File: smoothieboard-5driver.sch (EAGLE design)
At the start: 234 parts, among them IC1 LPC1769, IC10 LM1117-3.3V, IC11 78L12F, IC2 A4982, IC3 A4982, IC4 MCP44X1, IC5 A4982, IC6 A4982, J10 POWER_JACKSMD, Q1 BSL207SP, Q2 12MHz, Q3 25MHz, Q6 AOT240L, Q7 AOT240L, Q8 ZXMN4A06GTA, Q9 ZXMN4A06GTA, U1 USD-SOCKETNEW, X14 USBPTH

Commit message: Added 5th driver, 2nd digipot. Still lots of layout work to do
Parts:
- added C68, C69, C70, C71, C73: .1uF, rcl:C-EUC0603
- added C72: .22uF, rcl:C-EUC0603
- added C74: 100uF, SparkFun:CAP_POLE
- added IC12: A4982, A4982:A4982
- added IC9: MCP44X1, Geos:MCP44X1
- added J5: (no value), con-amp:MTA04-100
- added R18: 33K, resistor:R-US_R0603
- added R19, R20, R81: 10K, resistor:R-US_R0603
- added R21, R79: 0.05R, SparkFun:RESISTOR2512
- added R4: 100K, resistor:R-US_R0603
- added R80: NP, resistor:R-US_R0603
- added X5: (no value), con-weidmueller-sl35:180G-4
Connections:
- new net DIR5: IC12.DIR
- new net EN5: IC12.^EN
- new net N$29: IC9.!RESET, R4.1
- new net N$56: IC9.P0A, IC9.P1A, IC9.P2A, IC9.P3A, R18.1
- new net N$58: C69.2, IC12.CP1
- new net N$59: C69.1, IC12.CP2
- new net N$64: C70.2, IC12.VCP
- new net N$65: IC12.SENSE1, R21.2
- new net N$66: IC12.SENSE2, R79.2
- new net N$70: IC12.OUT1A, J5.2, X5.2
- new net N$71: IC12.OUT1B, J5.1, X5.1
- new net N$72: IC12.OUT2A, J5.3, X5.3
- new net N$76: IC12.OUT2B, J5.4, X5.4
- new net N$79: IC12.ROSC, R19.1, R80.1
- new net N$83: C72.2, IC12.VREG
- new net N$89: IC12.^SLEEP, R20.1
- new net N$95: IC12.^RESET, R81.1
- new net PW5: IC12.REF, IC9.P0W
- new net STEP5: IC12.STEP
- net 3.3V: now also C68.2, C71.1, IC12.VDD, IC9.HVC/A0, IC9.VDD, R18.2, R20.2, R4.2, R80.2, R81.2
- net GND: now also C68.1, C71.2, C72.1, C73.2, C74.-, IC12.GND1, IC12.GND2, IC12.PAD, IC9.A1, IC9.P0B, IC9.P1B, IC9.P2B, IC9.P3B, IC9.VSS, R19.2, R21.1, R79.1
- net MS1: now also IC12.MS1
- net MS2: now also IC12.MS2
- net POT_SCL: now also IC9.SCL
- net POT_SDA: now also IC9.SDA
- net VBB: now also C70.1, C73.1, C74.+, IC12.VBB1, IC12.VBB2

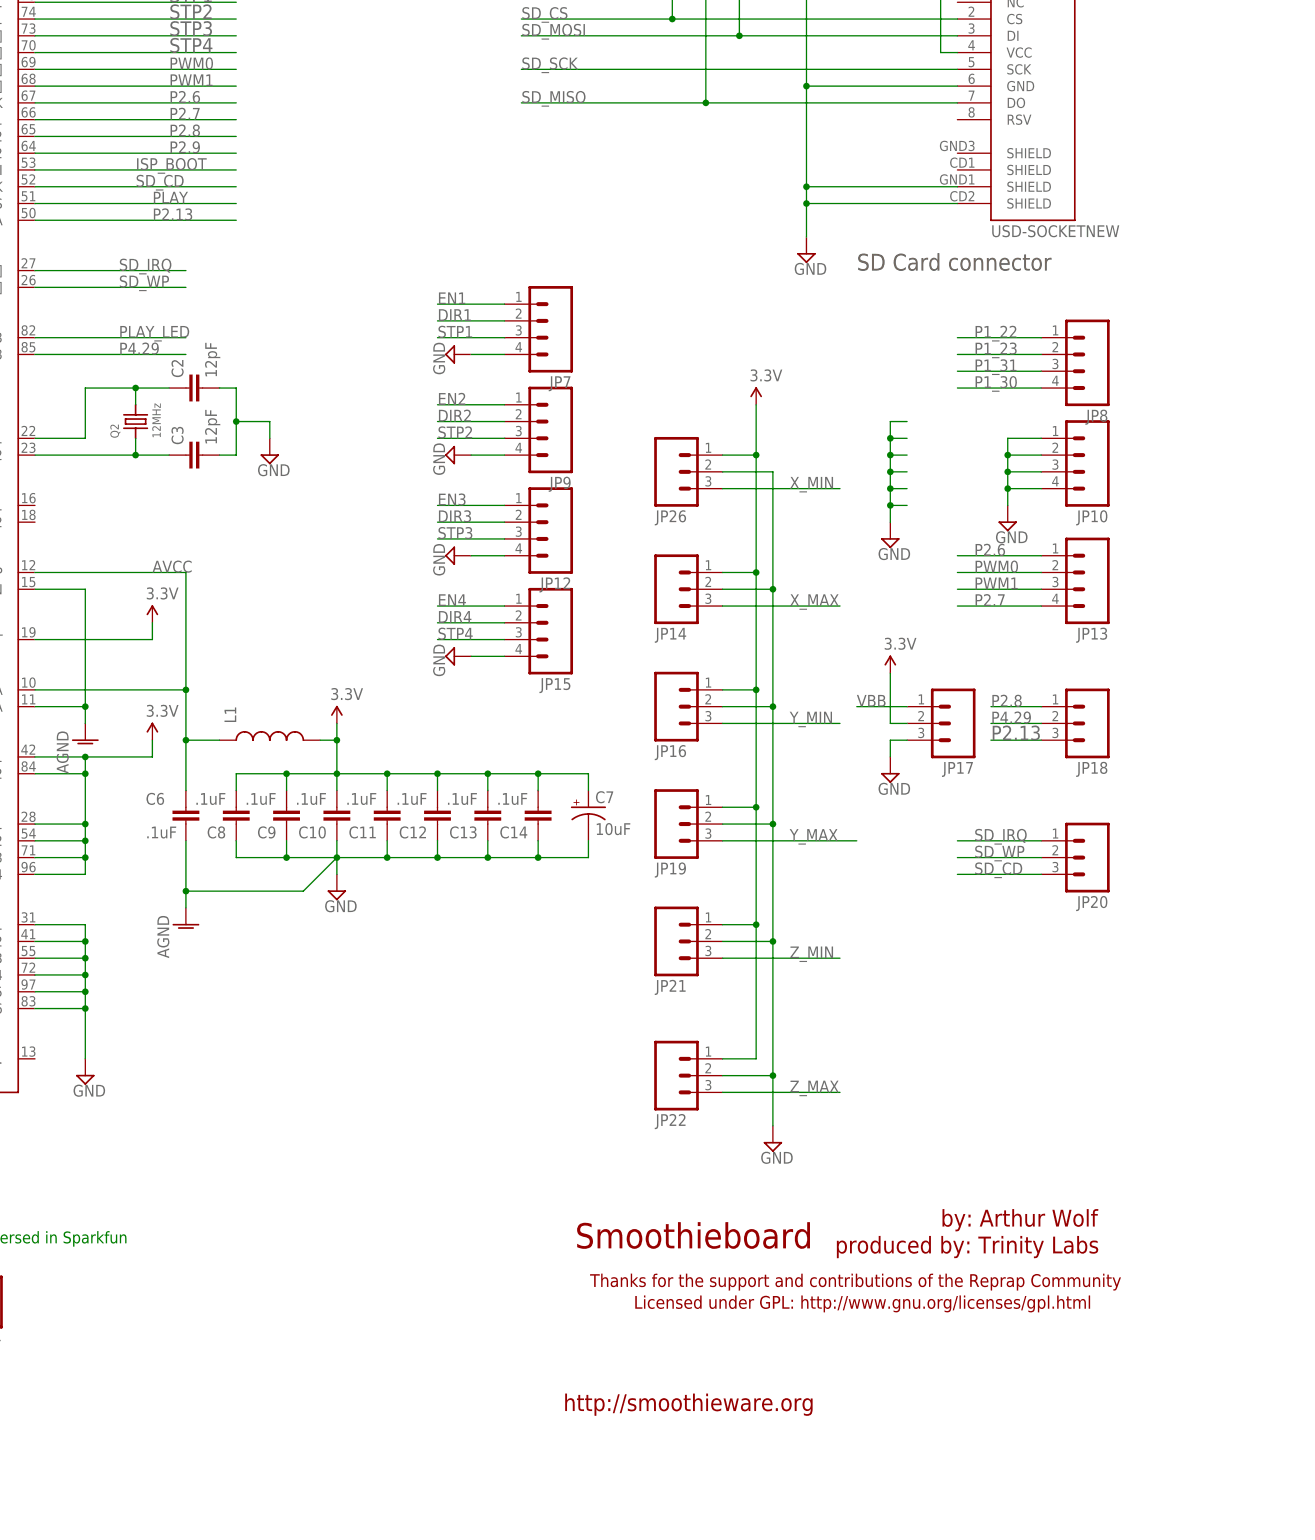
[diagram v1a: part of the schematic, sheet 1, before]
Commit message: shifted power connectors, lots of rearranging, still more to do
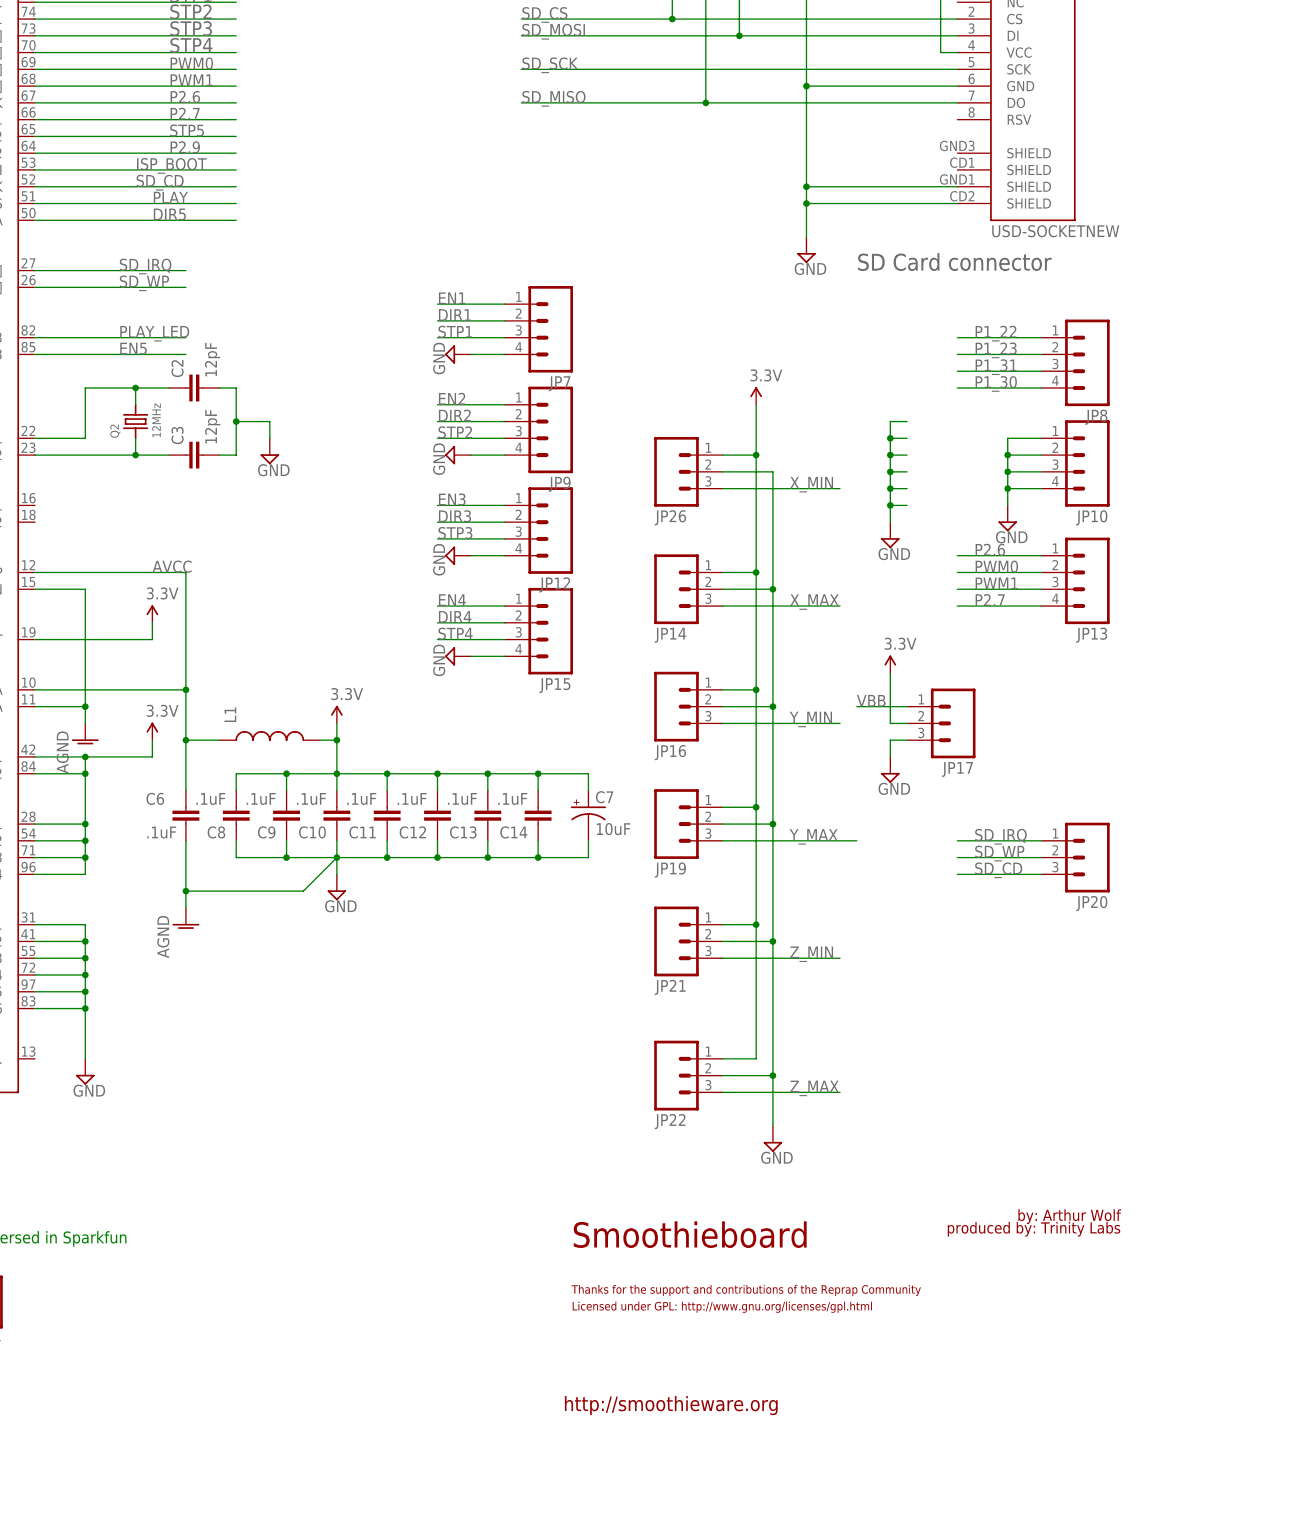
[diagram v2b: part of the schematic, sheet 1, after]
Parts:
- removed JP18: (no value), SparkFun:M03PTH
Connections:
- removed net P2.13: IC1.P2[13]/EINT3/I2STX_SDA, JP18.3
- removed net P2.8: IC1.P2[8]/TD2/TXD2, JP18.1
- removed net P4.29: IC1.P4[29]/TX_MCLK/MAT2[1]/RXD3, JP18.2
- removed net STEP5: IC12.STEP
- new net STP5: IC1.P2[8]/TD2/TXD2, IC12.STEP
- net DIR5: now also IC1.P2[13]/EINT3/I2STX_SDA
- net EN5: now also IC1.P4[29]/TX_MCLK/MAT2[1]/RXD3
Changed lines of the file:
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@@
 <setting verticaltext="up"/>
 </settings>
-<grid distance="0.1" unitdist="inch" unit="inch" style="lines" multiple="1" display="no" altdistance="0.01" altunitdist="inch" altunit="inch"/>
+<grid distance="25" unitdist="mil" unit="mil" style="lines" multiple="4" display="no" altdistance="0.01" altunitdist="inch" altunit="inch"/>
 <layers>
 <layer number="1" name="Top" color="4" fill="1" visible="no" active="no"/>
@@
 <part name="J9" library="con-amp" deviceset="MTA02-100" device=""/>
 <part name="JP17" library="SparkFun" deviceset="M03" device="PTH"/>
-<part name="JP18" library="SparkFun" deviceset="M03" device="PTH"/>
 <part name="SUPPLY37" library="supply2" deviceset="GND" device=""/>
 <part name="P+20" library="SparkFun" deviceset="3.3V" device=""/>
@@
 <text x="12.7" y="187.96" size="2.54" layer="97">UART0</text>
 <text x="12.7" y="182.88" size="2.54" layer="97">(Also for ISP Loading)</text>
-<text x="298.45" y="5.08" size="2.54" layer="94">http://smoothieware.org</text>
-<rectangle x1="342.9" y1="5.08" x2="383.54" y2="7.62" layer="210"/>
+<text x="298.45" y="5.08" size="2.1844" layer="94">http://smoothieware.org</text>
 <rectangle x1="342.9" y1="4.318" x2="383.286" y2="8.128" layer="210"/>
 <text x="200.66" y="30.48" size="1.778" layer="91">Symbol reversed in Sparkfun</text>
-<text x="300.228" y="29.718" size="3.81" layer="94">Smoothieboard</text>
-<text x="355.6" y="33.02" size="2.54" layer="94">by: Arthur Wolf</text>
-<text x="339.598" y="28.956" size="2.54" layer="94">produced by: Trinity Labs</text>
-<text x="309.118" y="20.574" size="1.9304" layer="94">Licensed under GPL: http://www.gnu.org/licenses/gpl.html</text>
-<text x="302.514" y="23.876" size="1.9304" layer="94">Thanks for the support and contributions of the Reprap Community</text>
+<text x="299.72" y="29.845" size="3.81" layer="94">Smoothieboard</text>
+<text x="382.905" y="35.56" size="1.6764" layer="94" rot="R180">by: Arthur Wolf</text>
+<text x="382.905" y="33.655" size="1.6764" layer="94" rot="R180">produced by: Trinity Labs</text>
+<text x="299.72" y="20.32" size="1.27" layer="94">Licensed under GPL: http://www.gnu.org/licenses/gpl.html</text>
+<text x="299.72" y="22.86" size="1.27" layer="94">Thanks for the support and contributions of the Reprap Community</text>
 </plain>
 <instances>
@@
 <instance part="JP23" gate="G$1" x="167.64" y="22.86" rot="MR180"/>
 <instance part="JP17" gate="G$1" x="358.14" y="109.22" rot="R180"/>
-<instance part="JP18" gate="G$1" x="378.46" y="109.22" rot="R180"/>
 <instance part="SUPPLY37" gate="GND" x="347.98" y="101.6"/>
 <instance part="P+20" gate="G$1" x="347.98" y="116.84"/>
@@
 </segment>
 </net>
-<net name="P2.8" class="0">
+<net name="STP5" class="0">
 <segment>
 <wire x1="218.44" y1="198.12" x2="248.92" y2="198.12" width="0.1524" layer="91"/>
@@
 <pinref part="IC1" gate="G$1" pin="P2[8]/TD2/TXD2"/>
 </segment>
-<segment>
-<wire x1="370.84" y1="111.76" x2="363.22" y2="111.76" width="0.1524" layer="91"/>
-<label x="363.22" y="111.76" size="1.778" layer="95"/>
-<pinref part="JP18" gate="G$1" pin="1"/>
-</segment>
 </net>
 <net name="P2.9" class="0">
@@
 </segment>
 </net>
-<net name="P2.13" class="0">
+<net name="DIR5" class="0">
 <segment>
 <wire x1="218.44" y1="185.42" x2="248.92" y2="185.42" width="0.1524" layer="91"/>
@@
 <pinref part="IC1" gate="G$1" pin="P2[13]/EINT3/I2STX_SDA"/>
 </segment>
-<segment>
-<wire x1="363.22" y1="106.68" x2="370.84" y2="106.68" width="0.1524" layer="91"/>
-<label x="363.22" y="106.68" size="2.1844" layer="95"/>
-<pinref part="JP18" gate="G$1" pin="3"/>
-</segment>
 </net>
-<net name="P4.29" class="0">
+<net name="EN5" class="0">
 <segment>
 <wire x1="218.44" y1="165.1" x2="241.3" y2="165.1" width="0.1524" layer="91"/>
@@
 <pinref part="IC1" gate="G$1" pin="P4[29]/TX_MCLK/MAT2[1]/RXD3"/>
 </segment>
-<segment>
-<wire x1="370.84" y1="109.22" x2="363.22" y2="109.22" width="0.1524" layer="91"/>
-<label x="363.22" y="109.22" size="1.778" layer="95"/>
-<pinref part="JP18" gate="G$1" pin="2"/>
-</segment>
 </net>
 <net name="X_MAX" class="0">
@@
 <text x="99.06" y="129.54" size="2.1844" layer="97">16 th</text>
 <text x="320.04" y="243.84" size="1.778" layer="97">Thermistor Connection</text>
-<text x="298.196" y="5.334" size="2.54" layer="94">http://smoothieware.org</text>
-<rectangle x1="342.9" y1="5.08" x2="383.54" y2="7.62" layer="210"/>
+<text x="298.196" y="5.334" size="2.1844" layer="94">http://smoothieware.org</text>
+<rectangle x1="342.265" y1="4.445" x2="382.905" y2="8.255" layer="210"/>
 </plain>
 <instances>
@@
 <sheet>
 <plain>
-<wire x1="342.9" y1="3.81" x2="383.54" y2="3.81" width="0.1524" layer="94"/>
-<wire x1="383.54" y1="8.128" x2="383.54" y2="3.81" width="0.1524" layer="94"/>
-<wire x1="342.9" y1="3.81" x2="383.54" y2="3.81" width="0.1524" layer="97"/>
-<wire x1="383.54" y1="3.81" x2="383.54" y2="8.128" width="0.1524" layer="97"/>
 <text x="317.5" y="134.62" size="2.54" layer="97">JP13,14   1-2: EXT FET- PS2</text>
 <text x="332.74" y="129.54" size="2.54" layer="97">2-3: VBB </text>
@@
 <text x="322.58" y="35.56" size="2.54" layer="97">GPIO Channel</text>
 <text x="284.48" y="35.56" size="2.54" layer="97">PWM Channel</text>
-<text x="321.31" y="14.986" size="2.54" layer="94">SmoothieBoard   ver 1.0</text>
-<text x="298.958" y="5.08" size="2.54" layer="94">http://smoothieware.org</text>
-<rectangle x1="297.18" y1="15.24" x2="307.34" y2="17.78" layer="210"/>
-<rectangle x1="342.9" y1="2.54" x2="383.54" y2="7.62" layer="210"/>
+<text x="298.45" y="32.766" size="2.54" layer="94">SmoothieBoard   ver 1.0</text>
+<text x="298.958" y="5.08" size="2.1844" layer="94">http://smoothieware.org</text>
+<rectangle x1="342.265" y1="4.445" x2="382.905" y2="8.255" layer="210"/>
 </plain>
 <instances>
@@
 <sheet>
 <plain>
+<text x="298.958" y="5.08" size="2.1844" layer="94">http://smoothieware.org</text>
+<rectangle x1="342.265" y1="4.445" x2="382.905" y2="8.255" layer="210"/>
 </plain>
 <instances>
@@
 </segment>
 </net>
-<net name="STEP5" class="0">
+<net name="STP5" class="0">
 <segment>
 <pinref part="IC12" gate="G$1" pin="STEP"/>

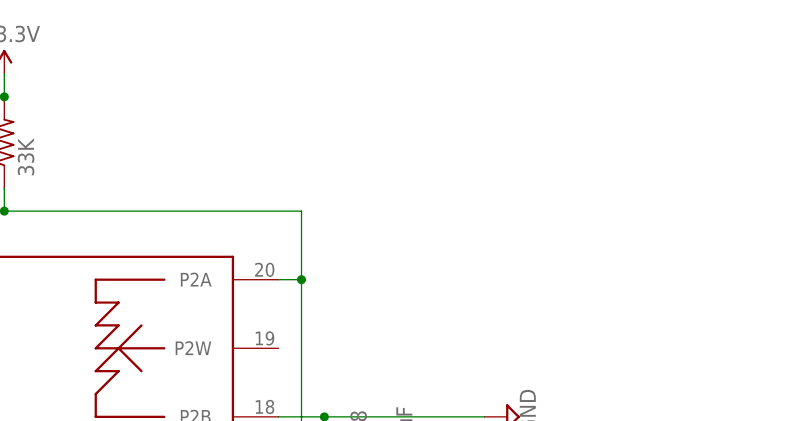
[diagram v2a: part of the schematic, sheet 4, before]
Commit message: added 1x4 connector for 5th driver en/dir/step signals to match other drivers
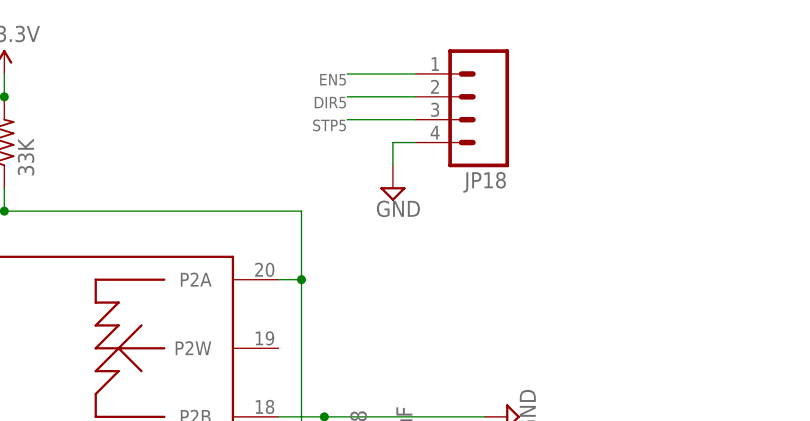
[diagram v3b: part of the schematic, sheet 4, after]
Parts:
- added JP18: (no value), SparkFun:M041X04_NO_SILK
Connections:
- net DIR5: now also JP18.2
- net EN5: now also JP18.1
- net GND: now also JP18.4
- net STP5: now also JP18.3
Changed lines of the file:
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@@
 <setting verticaltext="up"/>
 </settings>
-<grid distance="25" unitdist="mil" unit="mil" style="lines" multiple="4" display="no" altdistance="0.01" altunitdist="inch" altunit="inch"/>
+<grid distance="100" unitdist="mil" unit="mil" style="lines" multiple="1" display="no" altdistance="0.01" altunitdist="inch" altunit="inch"/>
 <layers>
 <layer number="1" name="Top" color="4" fill="1" visible="no" active="no"/>
@@
 <part name="R81" library="resistor" deviceset="R-US_" device="R0603" value="10K"/>
 <part name="C74" library="SparkFun" deviceset="CAP_POL" device="E" value="100uF"/>
+<part name="JP18" library="SparkFun" deviceset="M04" device="1X04_NO_SILK"/>
+<part name="SUPPLY81" library="supply2" deviceset="GND" device=""/>
 </parts>
 <sheets>
@@
 <instance part="R81" gate="G$1" x="38.1" y="121.92" rot="R90"/>
 <instance part="C74" gate="G$1" x="101.6" y="81.28"/>
+<instance part="JP18" gate="G$1" x="106.68" y="243.84" rot="R180"/>
+<instance part="SUPPLY81" gate="GND" x="99.06" y="233.68"/>
 </instances>
 <busses>
@@
 <pinref part="SUPPLY80" gate="GND" pin="GND"/>
 </segment>
+<segment>
+<pinref part="JP18" gate="G$1" pin="4"/>
+<pinref part="SUPPLY81" gate="GND" pin="GND"/>
+<wire x1="99.06" y1="236.22" x2="99.06" y2="238.76" width="0.1524" layer="91"/>
+<wire x1="99.06" y1="238.76" x2="101.6" y2="238.76" width="0.1524" layer="91"/>
+</segment>
 </net>
 <net name="N$29" class="0">
@@
 <label x="22.86" y="93.98" size="1.778" layer="95" rot="R180"/>
 </segment>
+<segment>
+<pinref part="JP18" gate="G$1" pin="1"/>
+<wire x1="101.6" y1="246.38" x2="93.98" y2="246.38" width="0.1524" layer="91"/>
+<label x="93.98" y="246.38" size="1.27" layer="95" rot="R180"/>
+</segment>
 </net>
 <net name="STP5" class="0">
@@
 <label x="22.86" y="88.9" size="1.778" layer="95" rot="R180"/>
 </segment>
+<segment>
+<pinref part="JP18" gate="G$1" pin="3"/>
+<wire x1="101.6" y1="241.3" x2="93.98" y2="241.3" width="0.1524" layer="91"/>
+<label x="93.98" y="241.3" size="1.27" layer="95" rot="R180"/>
+</segment>
 </net>
 <net name="DIR5" class="0">
@@
 <label x="22.86" y="86.36" size="1.778" layer="95" rot="R180"/>
 </segment>
+<segment>
+<pinref part="JP18" gate="G$1" pin="2"/>
+<wire x1="101.6" y1="243.84" x2="93.98" y2="243.84" width="0.1524" layer="91"/>
+<label x="93.98" y="243.84" size="1.27" layer="95" rot="R180"/>
+</segment>
 </net>

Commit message: Gave small mosfets more heatsink area, moved some signal traces from bottom layer to route15 to improve stepper driver cooling, lots of other tweaks
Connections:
- net N$18 renamed SMALL_MOSFET_POWER
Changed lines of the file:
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@@
 </segment>
 </net>
-<net name="N$52" class="0">
+<net name="N$18" class="0">
 <segment>
 <wire x1="271.78" y1="78.74" x2="271.78" y2="83.82" width="0.4064" layer="91"/>
@@
 </segment>
 </net>
-<net name="N$18" class="0">
+<net name="SMALL_MOSFET_POWER" class="0">
 <segment>
 <wire x1="220.98" y1="121.92" x2="223.52" y2="121.92" width="0.4064" layer="91"/>
